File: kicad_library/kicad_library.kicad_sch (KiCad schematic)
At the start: 0 parts

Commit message: added default footprint to wire and jack pad
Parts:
- added U1: ~, symbol wire_pad:wire_pad
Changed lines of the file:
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@@
 (kicad_sch (version 20230121) (generator eeschema)
   (paper "A4")
+  (symbol (lib_id "wire_pad:wire_pad") (at 130.81 45.72 0) (unit 1)
+    (in_bom yes) (on_board yes) (dnp no) (fields_autoplaced)
+    (property "Reference" "U1" (at 130.81 41.91 0) (do_not_autoplace)
+      (effects (font (size 1.27 1.27)))
+    )
+    (property "Value" "~" (at 130.81 45.72 0)
+      (effects (font (size 1.27 1.27)))
+    )
+    (property "Footprint" "" (at 130.81 45.72 0)
+      (effects (font (size 1.27 1.27)) hide)
+    )
+    (property "Datasheet" "" (at 130.81 45.72 0)
+      (effects (font (size 1.27 1.27)) hide)
+    )
+    (pin "1")
+    (instances
+      (project "kicad_library"
+        (path "/187cd165-a145-4c34-82ff-b940576a2f8e"
+          (reference "U1") (unit 1)
+        )
+      )
+    )
+  )
   (sheet_instances
     (path "/" (page "1"))

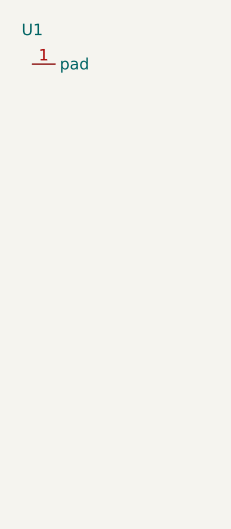
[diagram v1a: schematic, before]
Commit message: UPD: fixed footprint symbol association
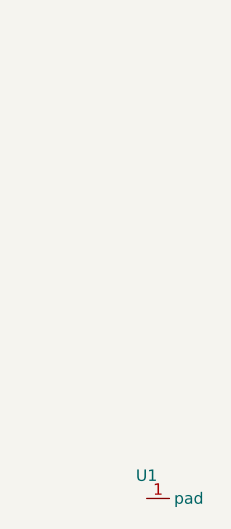
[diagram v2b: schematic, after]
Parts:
- removed U1: ~, symbol wire_pad:wire_pad
- added U1: ~, Library:jack_pad, symbol jack_pad:jack_pad
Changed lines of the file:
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@@
 (kicad_sch (version 20230121) (generator eeschema)
   (paper "A4")
-  (symbol (lib_id "wire_pad:wire_pad") (at 130.81 45.72 0) (unit 1)
+  (symbol (lib_id "jack_pad:jack_pad") (at 143.51 93.98 0) (unit 1)
     (in_bom yes) (on_board yes) (dnp no) (fields_autoplaced)
-    (property "Reference" "U1" (at 130.81 41.91 0) (do_not_autoplace)
+    (property "Reference" "U1" (at 143.51 91.44 0) (do_not_autoplace)
       (effects (font (size 1.27 1.27)))
     )
-    (property "Value" "~" (at 130.81 45.72 0)
+    (property "Value" "~" (at 143.51 93.98 0)
       (effects (font (size 1.27 1.27)))
     )
-    (property "Footprint" "" (at 130.81 45.72 0)
+    (property "Footprint" "Library:jack_pad" (at 143.51 93.98 0)
       (effects (font (size 1.27 1.27)) hide)
     )
-    (property "Datasheet" "" (at 130.81 45.72 0)
+    (property "Datasheet" "" (at 143.51 93.98 0)
       (effects (font (size 1.27 1.27)) hide)
     )

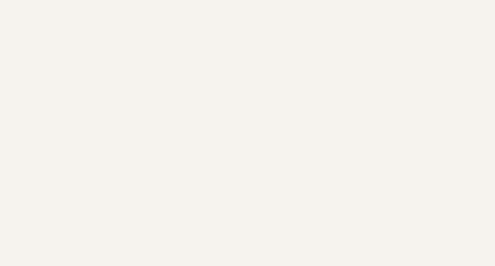
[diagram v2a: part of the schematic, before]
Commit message: UPD: Library add of 0ZCH0050FF2G
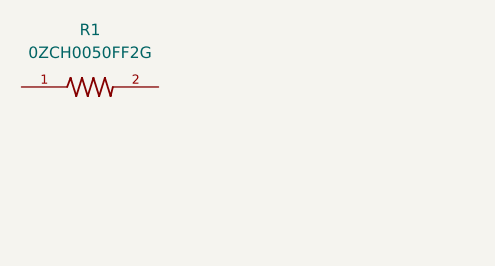
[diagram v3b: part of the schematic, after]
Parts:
- added R1: 0ZCH0050FF2G, 0ZCH0050FF2G:RESC3225X75N, symbol SBC_PTC_FUSE:0ZCH0050FF2G
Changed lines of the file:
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@@
 (kicad_sch (version 20230121) (generator eeschema)
   (paper "A4")
+  (symbol (lib_id "SBC_PTC_FUSE:0ZCH0050FF2G") (at 60.96 77.47 0) (unit 1)
+    (in_bom yes) (on_board yes) (dnp no) (fields_autoplaced)
+    (property "Reference" "R1" (at 60.96 71.12 0)
+      (effects (font (size 1.27 1.27)))
+    )
+    (property "Value" "0ZCH0050FF2G" (at 60.96 73.66 0)
+      (effects (font (size 1.27 1.27)))
+    )
+    (property "Footprint" "0ZCH0050FF2G:RESC3225X75N" (at 60.96 73.66 0)
+      (effects (font (size 1.27 1.27)) (justify bottom) hide)
+    )
+    (property "Datasheet" "" (at 60.96 77.47 0)
+      (effects (font (size 1.27 1.27)) hide)
+    )
+    (property "PARTREV" "0ZCH Sep2019" (at 60.96 71.12 0)
+      (effects (font (size 1.27 1.27)) (justify bottom) hide)
+    )
+    (property "MANUFACTURER" "Bel Fuse" (at 60.96 68.58 0)
+      (effects (font (size 1.27 1.27)) (justify bottom) hide)
+    )
+    (property "MAXIMUM_PACKAGE_HEIGHT" "0.75mm" (at 60.96 83.82 0)
+      (effects (font (size 1.27 1.27)) (justify bottom) hide)
+    )
+    (property "STANDARD" "IPC-7351B" (at 60.96 86.36 0)
+      (effects (font (size 1.27 1.27)) (justify bottom) hide)
+    )
+    (pin "1")
+    (pin "2")
+    (instances
+      (project "kicad_library"
+        (path "/187cd165-a145-4c34-82ff-b940576a2f8e"
+          (reference "R1") (unit 1)
+        )
+      )
+    )
+  )
   (symbol (lib_id "jack_pad:jack_pad") (at 143.51 93.98 0) (unit 1)
     (in_bom yes) (on_board yes) (dnp no) (fields_autoplaced)
